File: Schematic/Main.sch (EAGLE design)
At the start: 54 parts, among them IC1 PIC18F4550_40, IC2 7805, IC4 AD7734, IC5 AD780, K1 SRD-24VDC-SL-C, K2 SRD-24VDC-SL-C, Q1 20MHz, Q2 3.579545MHz, T1 2N2222, U1 LM317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

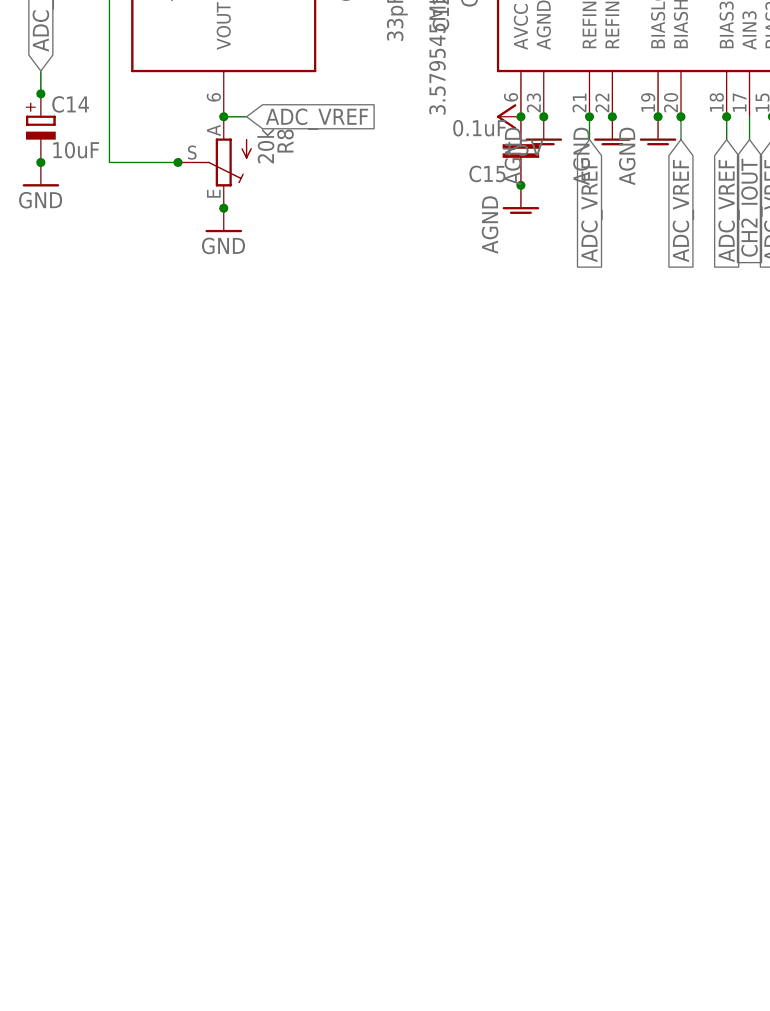
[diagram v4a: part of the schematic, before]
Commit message: Added voltage out resistor dividers.
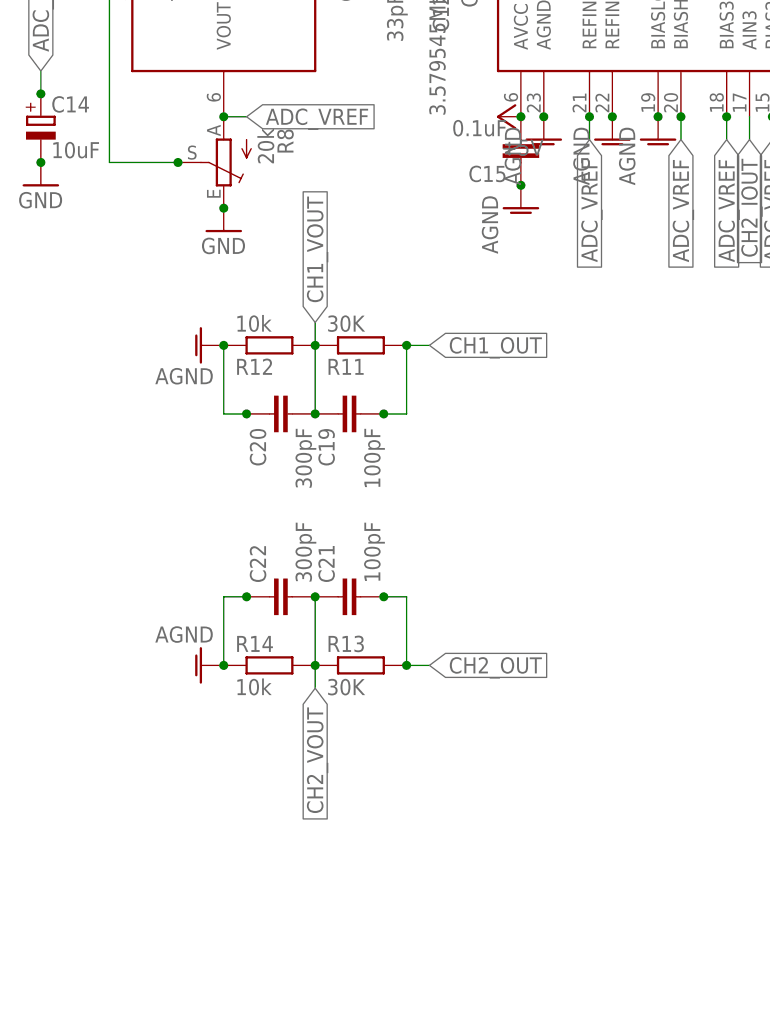
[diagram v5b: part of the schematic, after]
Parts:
- added C19, C21: 100pF, rcl:C-EU025-030X050
- added C20, C22: 300pF, rcl:C-EU025-030X050
- added R11, R13: 30K, rcl:R-EU_0204/7
- added R12, R14: 10k, rcl:R-EU_0204/7
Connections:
- removed net N$28: C7.+, D4.C, IC3.IP+0, IC3.IP+1, K2.IN
- new net CH1_OUT: C19.2, C7.+, D4.C, IC3.IP+0, IC3.IP+1, K2.IN, R11.2
- new net CH2_OUT: C21.2, R13.2
- net AGND: now also C20.1, C22.1, R12.1, R14.1
- net CH1_VOUT: now also C19.1, C20.2, R11.1, R12.2
- net CH2_VOUT: now also C21.1, C22.2, R13.1, R14.2
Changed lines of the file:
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@@
 <part name="D4" library="diode" deviceset="1N4148" device="DO35-7" value="1N4148"/>
 <part name="GNDI4" library="supply1" deviceset="GNDI" device=""/>
+<part name="R11" library="rcl" deviceset="R-EU_" device="0204/7" value="30K"/>
+<part name="R12" library="rcl" deviceset="R-EU_" device="0204/7" value="10k"/>
+<part name="AGND8" library="supply1" deviceset="AGND" device=""/>
+<part name="C19" library="rcl" deviceset="C-EU" device="025-030X050" value="100pF"/>
+<part name="C20" library="rcl" deviceset="C-EU" device="025-030X050" value="300pF"/>
+<part name="R13" library="rcl" deviceset="R-EU_" device="0204/7" value="30K"/>
+<part name="R14" library="rcl" deviceset="R-EU_" device="0204/7" value="10k"/>
+<part name="AGND9" library="supply1" deviceset="AGND" device=""/>
+<part name="C21" library="rcl" deviceset="C-EU" device="025-030X050" value="100pF"/>
+<part name="C22" library="rcl" deviceset="C-EU" device="025-030X050" value="300pF"/>
 </parts>
 <sheets>
@@
 <instance part="D4" gate="G$1" x="5.08" y="-86.36" rot="R270"/>
 <instance part="GNDI4" gate="G$1" x="5.08" y="-81.28" rot="R180"/>
+<instance part="R11" gate="G$1" x="-139.7" y="-58.42" rot="MR180"/>
+<instance part="R12" gate="G$1" x="-149.86" y="-58.42" rot="MR180"/>
+<instance part="AGND8" gate="VR1" x="-157.48" y="-58.42" rot="MR90"/>
+<instance part="C19" gate="G$1" x="-142.24" y="-66.04" rot="MR270"/>
+<instance part="C20" gate="G$1" x="-149.86" y="-66.04" rot="MR270"/>
+<instance part="R13" gate="G$1" x="-139.7" y="-93.98"/>
+<instance part="R14" gate="G$1" x="-149.86" y="-93.98"/>
+<instance part="AGND9" gate="VR1" x="-157.48" y="-93.98" rot="R270"/>
+<instance part="C21" gate="G$1" x="-142.24" y="-86.36" rot="R90"/>
+<instance part="C22" gate="G$1" x="-149.86" y="-86.36" rot="R90"/>
 </instances>
 <busses>
@@
 </segment>
 </net>
-<net name="N$28" class="0">
-<segment>
-<pinref part="K2" gate="G$1" pin="IN"/>
-<pinref part="C7" gate="G$1" pin="+"/>
-<pinref part="IC3" gate="G$1" pin="IP+1"/>
-<wire x1="5.08" y1="-88.9" x2="7.62" y2="-88.9" width="0.1524" layer="91"/>
-<junction x="5.08" y="-88.9"/>
-<pinref part="IC3" gate="G$1" pin="IP+0"/>
-<junction x="7.62" y="-88.9"/>
-<wire x1="7.62" y1="-88.9" x2="15.24" y2="-88.9" width="0.1524" layer="91"/>
-<junction x="15.24" y="-88.9"/>
-<pinref part="D4" gate="G$1" pin="C"/>
-</segment>
-</net>
 <net name="N$29" class="0">
 <segment>
@@
 <junction x="-121.92" y="-40.64"/>
 </segment>
+<segment>
+<pinref part="R12" gate="G$1" pin="1"/>
+<pinref part="AGND8" gate="VR1" pin="AGND"/>
+<junction x="-154.94" y="-58.42"/>
+<pinref part="C20" gate="G$1" pin="1"/>
+<wire x1="-154.94" y1="-58.42" x2="-154.94" y2="-66.04" width="0.1524" layer="91"/>
+<wire x1="-154.94" y1="-66.04" x2="-152.4" y2="-66.04" width="0.1524" layer="91"/>
+<junction x="-152.4" y="-66.04"/>
+</segment>
+<segment>
+<pinref part="R14" gate="G$1" pin="1"/>
+<pinref part="AGND9" gate="VR1" pin="AGND"/>
+<junction x="-154.94" y="-93.98"/>
+<pinref part="C22" gate="G$1" pin="1"/>
+<wire x1="-154.94" y1="-93.98" x2="-154.94" y2="-86.36" width="0.1524" layer="91"/>
+<wire x1="-154.94" y1="-86.36" x2="-152.4" y2="-86.36" width="0.1524" layer="91"/>
+<junction x="-152.4" y="-86.36"/>
+</segment>
 </net>
 <net name="CH2_IOUT" class="0">
@@
 <junction x="-91.44" y="-33.02"/>
 </segment>
+<segment>
+<pinref part="R13" gate="G$1" pin="1"/>
+<pinref part="R14" gate="G$1" pin="2"/>
+<wire x1="-144.78" y1="-93.98" x2="-144.78" y2="-96.52" width="0.1524" layer="91"/>
+<label x="-144.78" y="-96.52" size="1.778" layer="95" rot="R270" xref="yes"/>
+<junction x="-144.78" y="-93.98"/>
+<pinref part="C22" gate="G$1" pin="2"/>
+<pinref part="C21" gate="G$1" pin="1"/>
+<wire x1="-144.78" y1="-86.36" x2="-144.78" y2="-93.98" width="0.1524" layer="91"/>
+<junction x="-144.78" y="-86.36"/>
+</segment>
 </net>
 <net name="CH1_VOUT" class="0">
@@
 <junction x="-81.28" y="-33.02"/>
 </segment>
-</net>
+<segment>
+<pinref part="R11" gate="G$1" pin="1"/>
+<pinref part="R12" gate="G$1" pin="2"/>
+<wire x1="-144.78" y1="-58.42" x2="-144.78" y2="-55.88" width="0.1524" layer="91"/>
+<label x="-144.78" y="-55.88" size="1.778" layer="95" rot="MR90" xref="yes"/>
+<junction x="-144.78" y="-58.42"/>
+<pinref part="C20" gate="G$1" pin="2"/>
+<pinref part="C19" gate="G$1" pin="1"/>
+<wire x1="-144.78" y1="-66.04" x2="-144.78" y2="-58.42" width="0.1524" layer="91"/>
+<junction x="-144.78" y="-66.04"/>
+</segment>
+</net>
+<net name="CH1_OUT" class="0">
+<segment>
+<pinref part="R11" gate="G$1" pin="2"/>
+<wire x1="-132.08" y1="-58.42" x2="-134.62" y2="-58.42" width="0.1524" layer="91"/>
+<label x="-132.08" y="-58.42" size="1.778" layer="95" rot="MR180" xref="yes"/>
+<junction x="-134.62" y="-58.42"/>
+<pinref part="C19" gate="G$1" pin="2"/>
+<wire x1="-137.16" y1="-66.04" x2="-134.62" y2="-66.04" width="0.1524" layer="91"/>
+<wire x1="-134.62" y1="-66.04" x2="-134.62" y2="-58.42" width="0.1524" layer="91"/>
+<junction x="-137.16" y="-66.04"/>
+</segment>
+<segment>
+<pinref part="K2" gate="G$1" pin="IN"/>
+<pinref part="C7" gate="G$1" pin="+"/>
+<pinref part="IC3" gate="G$1" pin="IP+1"/>
+<wire x1="5.08" y1="-88.9" x2="7.62" y2="-88.9" width="0.1524" layer="91"/>
+<junction x="5.08" y="-88.9"/>
+<pinref part="IC3" gate="G$1" pin="IP+0"/>
+<junction x="7.62" y="-88.9"/>
+<wire x1="7.62" y1="-88.9" x2="15.24" y2="-88.9" width="0.1524" layer="91"/>
+<junction x="15.24" y="-88.9"/>
+<pinref part="D4" gate="G$1" pin="C"/>
+</segment>
+</net>
+<net name="CH2_OUT" class="0">
+<segment>
+<pinref part="R13" gate="G$1" pin="2"/>
+<wire x1="-132.08" y1="-93.98" x2="-134.62" y2="-93.98" width="0.1524" layer="91"/>
+<label x="-132.08" y="-93.98" size="1.778" layer="95" xref="yes"/>
+<junction x="-134.62" y="-93.98"/>
+<pinref part="C21" gate="G$1" pin="2"/>
+<wire x1="-137.16" y1="-86.36" x2="-134.62" y2="-86.36" width="0.1524" layer="91"/>
+<wire x1="-134.62" y1="-86.36" x2="-134.62" y2="-93.98" width="0.1524" layer="91"/>
+<junction x="-137.16" y="-86.36"/>
+</segment>
+</net>

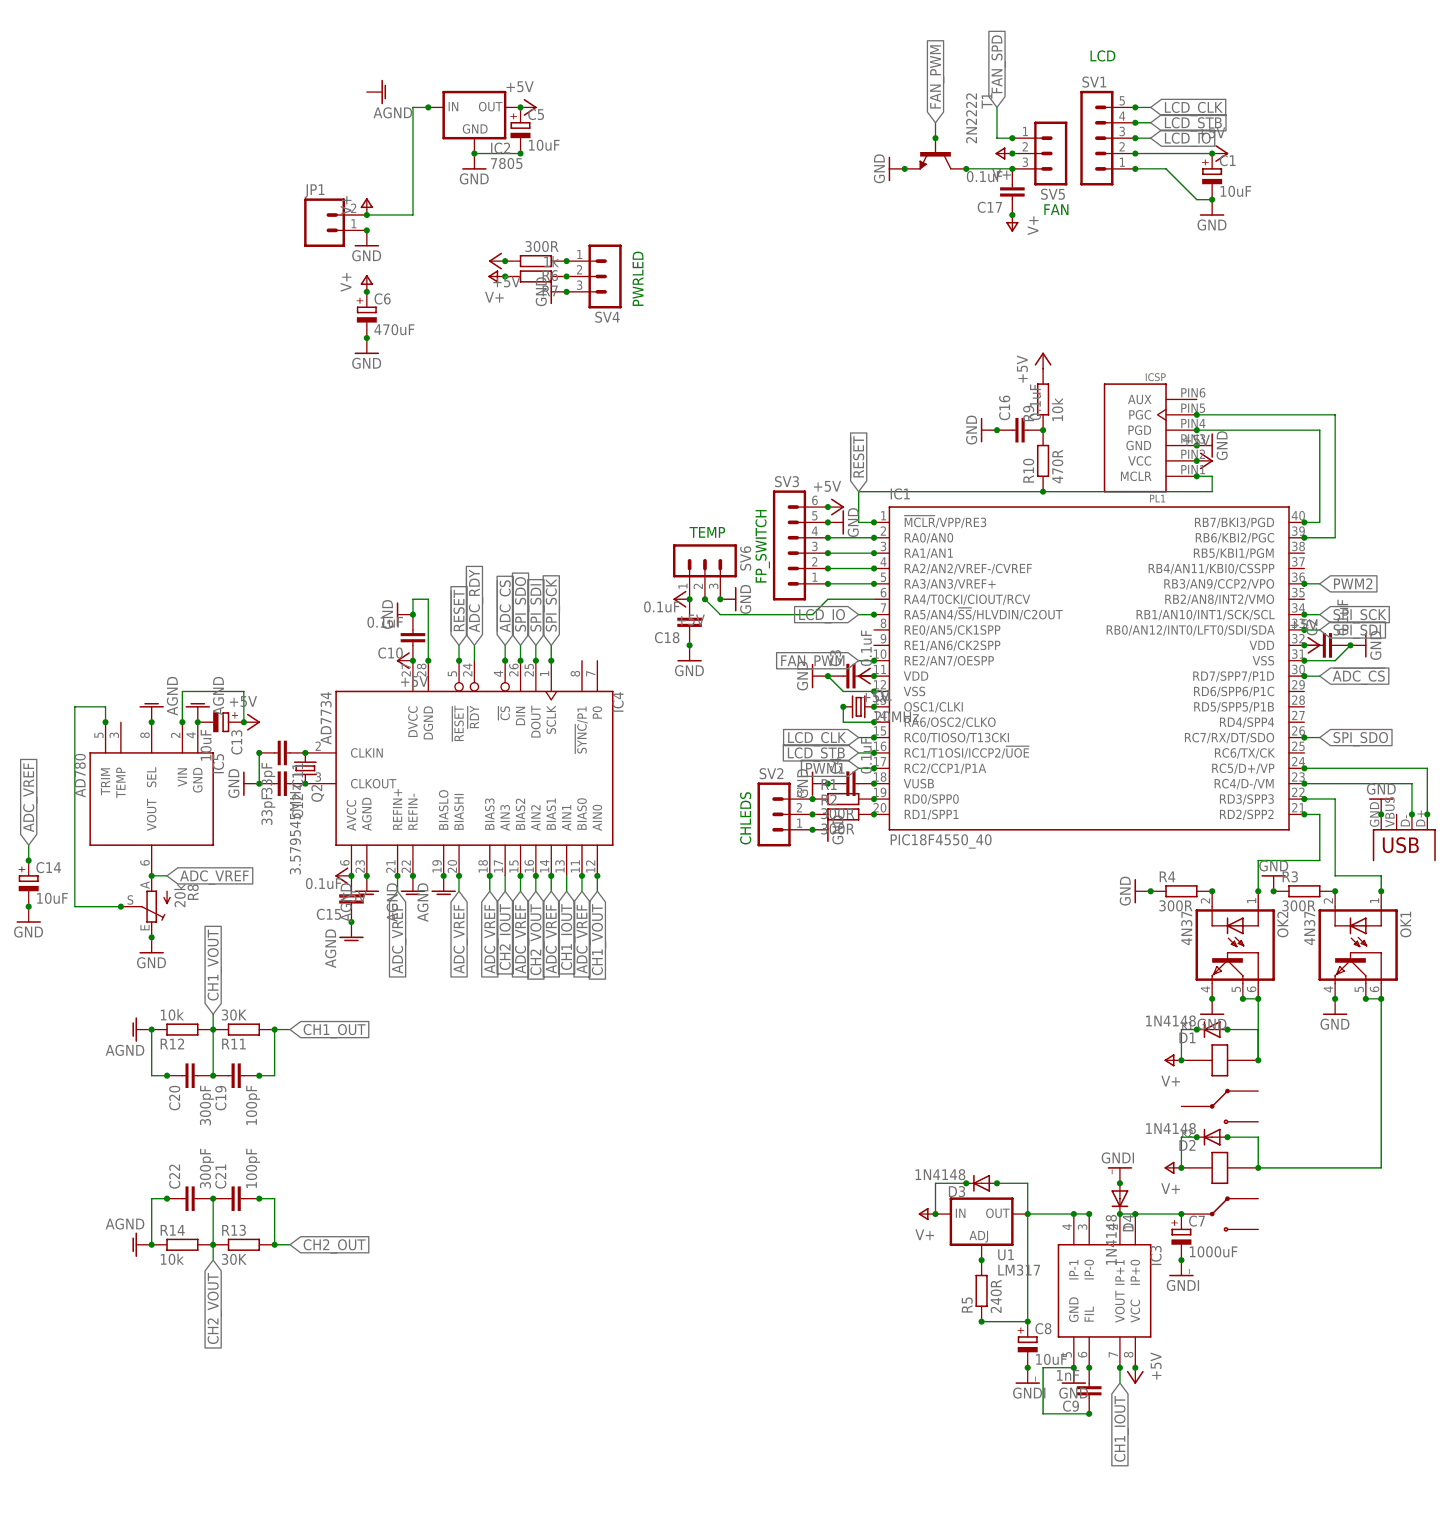
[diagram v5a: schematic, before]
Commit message: Added isolation between SPI lines and ADC
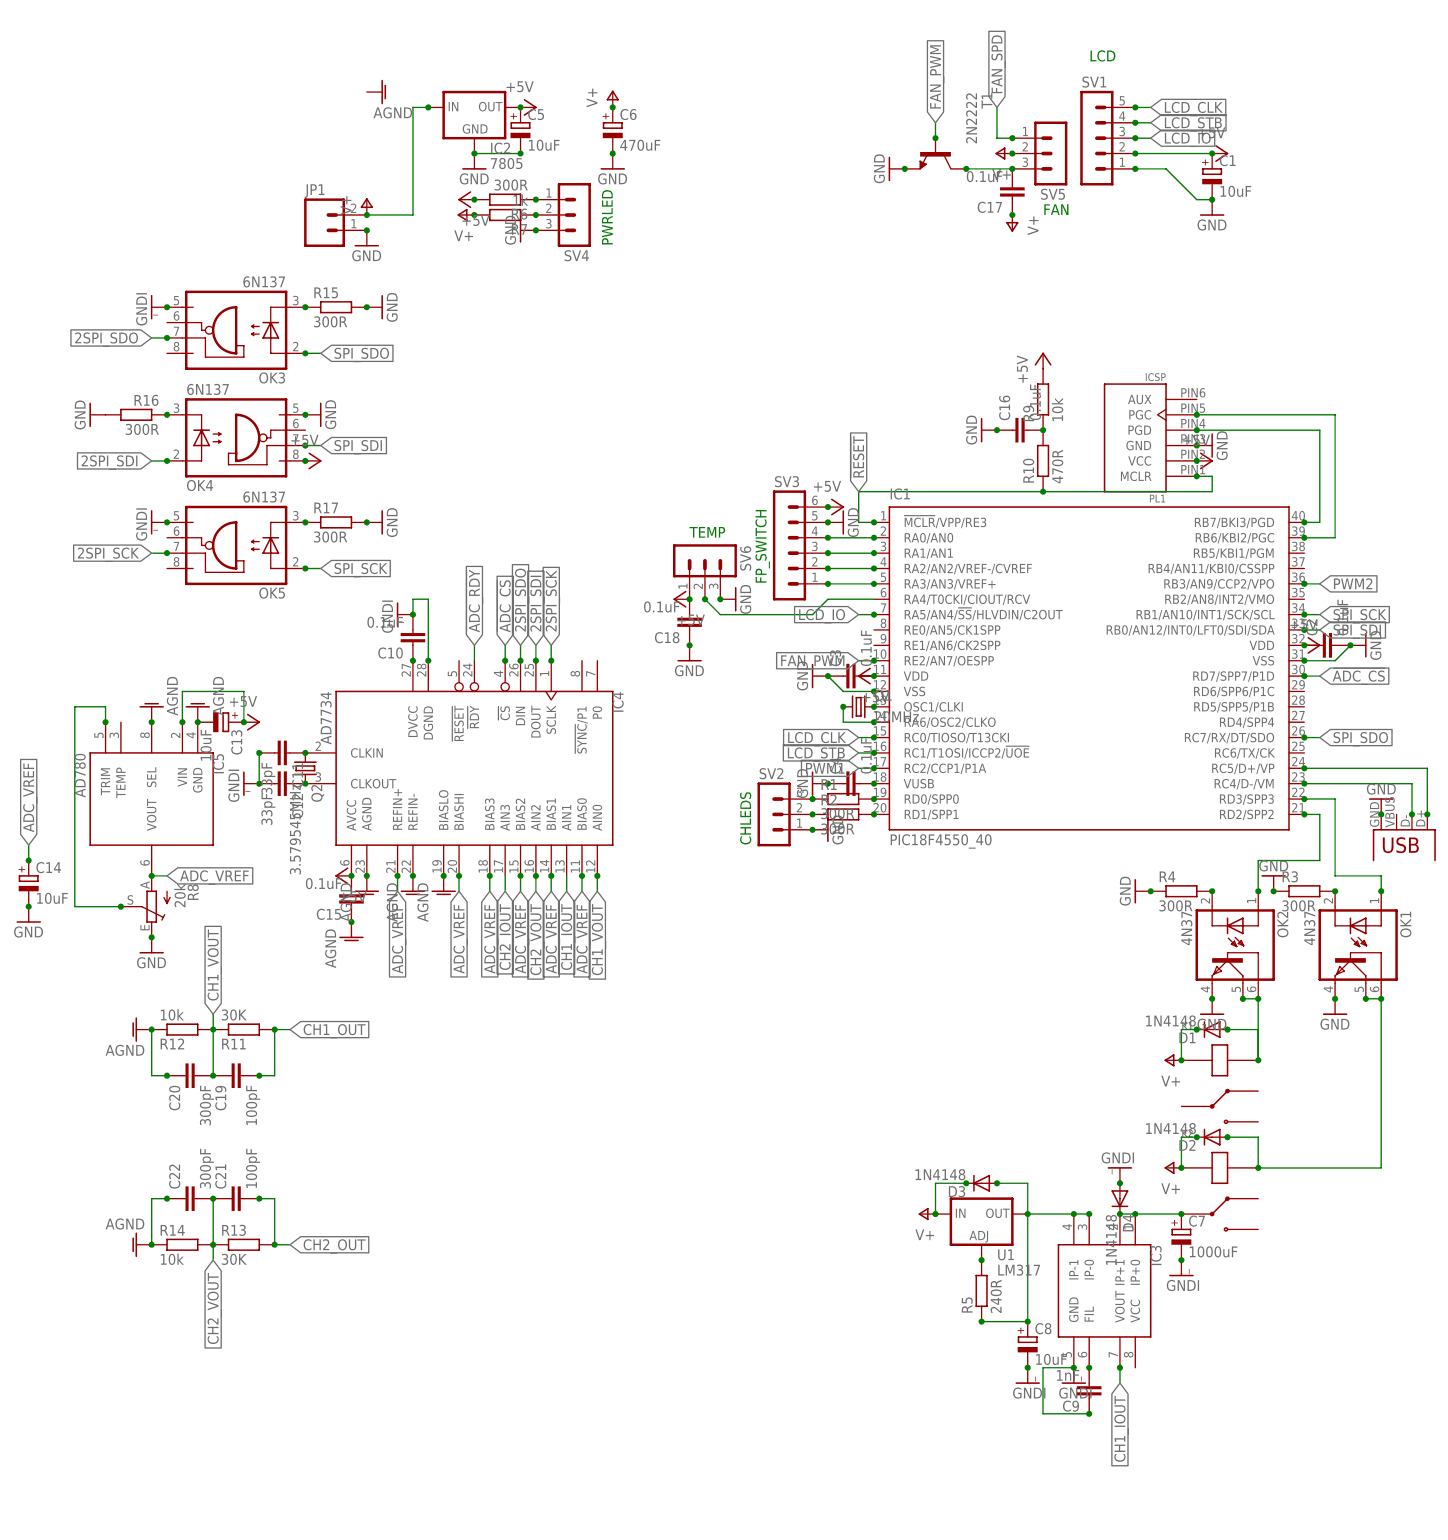
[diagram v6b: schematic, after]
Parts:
- added OK3, OK4, OK5: 6N137, Particulates:6N137
- added R15, R16, R17: 300R, rcl:R-EU_0204/7
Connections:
- new net 2SPI_SCK: IC4.SCLK, OK5.VE
- new net 2SPI_SDI: IC4.DOUT, OK4.A
- new net 2SPI_SDO: IC4.DIN, OK3.VE
- new net N$28: OK5.C, R17.1
- new net N$34: OK4.C, R16.1
- new net N$35: OK3.C, R15.1
- net !RESET!: no longer IC4.!RESET!
- net +5V: now also OK4.VCC; no longer IC3.VCC
- net GND: now also OK4.GND, R15.2, R16.2, R17.2; no longer C10.2, C11.2, C12.2, C9.1, IC3.GND, IC4.DGND
- net GNDI: now also C10.2, C11.2, C12.2, C9.1, IC3.GND, IC4.DGND, OK3.GND, OK5.GND
- net SPI_SCK: now also OK5.A; no longer IC4.SCLK
- net SPI_SDI: now also OK4.VE; no longer IC4.DOUT
- net SPI_SDO: now also OK3.A; no longer IC4.DIN
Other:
- moved on the sheet: C6, R6, R7, SV4
